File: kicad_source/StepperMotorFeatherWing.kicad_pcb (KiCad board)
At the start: 2 copper layers, 100 x 60 mm, 120 parts, among them CN1 ADAFRUIT_FEATHER, CN10 CONN_01X04, CN11 CONN_01X05, CN20 CONN_01X04, CN21 CONN_01X05, P1 WR-TBL_691322310002, P10 CONN_01X04, P2 WR-TBL_691313710002, P7 CONN_01X04, P8 CONN_01X04, P9 CONN_01X04, Q1 IPD90P03P4L- 04, U1 TMC5130A-TA, U2 TMC5130A-TA, U3 LT1085, U4 LM75, U9 IFX91041EJV, Y1 oscillator

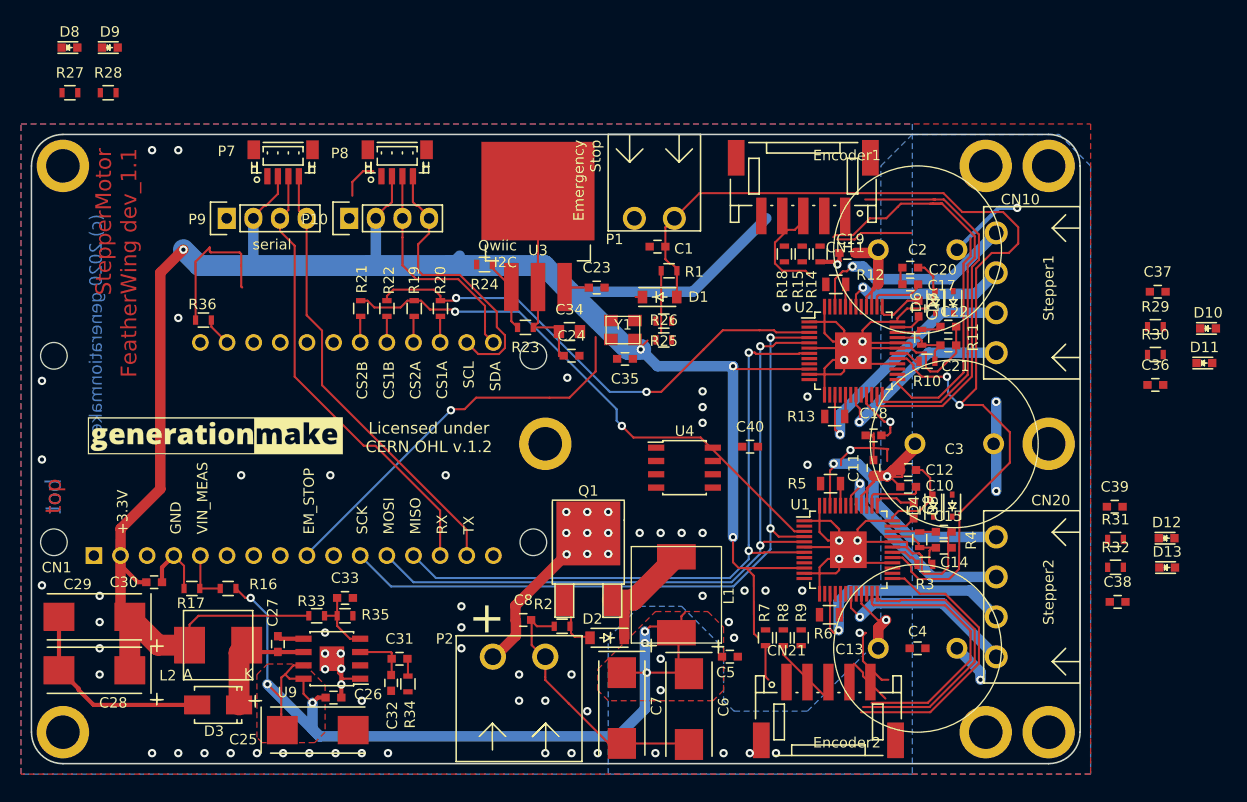
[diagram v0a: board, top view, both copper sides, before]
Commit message: updated layout
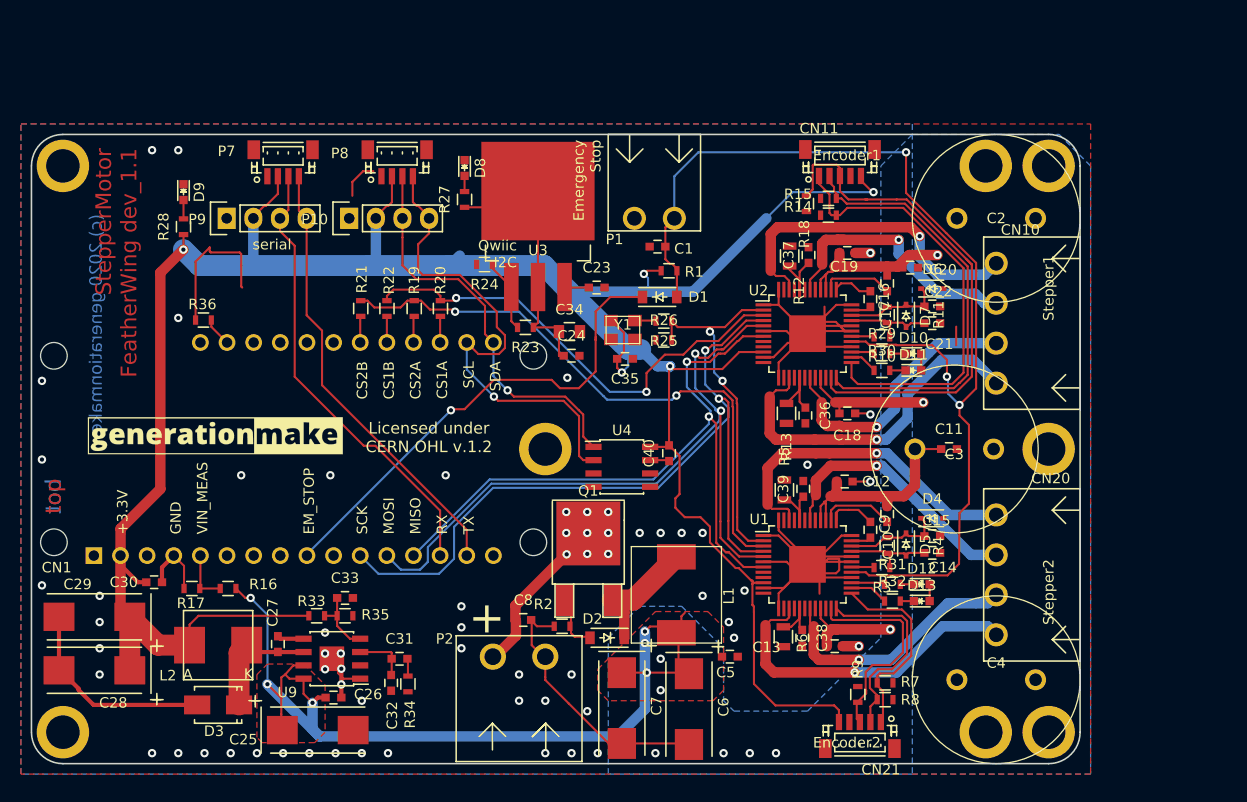
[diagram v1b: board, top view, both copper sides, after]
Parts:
- CN11, CN21: footprint connectors_JST_PH:Connectors_JST_S5B-PH-SM4-TB -> connectors_JST_SH:Connectors_JST_BM05B-SRSS-TB
- moved G*** 47.2 mm to (138.1, 62.4)
- moved D8 39.4 mm to (92.3, 69.2), turned to 270 degrees
- moved R27 39.0 mm to (92.3, 72.2), turned to 90 degrees
- moved C36 33.5 mm to (124.8, 92.8), turned to 270 degrees
- moved C37 33.5 mm to (125.1, 77.5), turned to 90 degrees
- moved C38 30.3 mm to (124.5, 114.0), turned to 270 degrees
- moved C39 29.7 mm to (124.6, 99.8), turned to 90 degrees
- moved D10 28.2 mm to (135.1, 86.9)
- moved D11 27.8 mm to (135.1, 88.5)
- moved R29 26.2 mm to (132.1, 86.9)
- moved R30 26.1 mm to (132.1, 88.5)
- moved D12 23.8 mm to (135.9, 108.9)
- moved D13 23.6 mm to (135.9, 110.5)
- moved R31 21.7 mm to (133.1, 108.9)
- moved R32 21.5 mm to (133.1, 110.5)
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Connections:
- CN10 pad 1: /MotorDriver1/OB2 -> /MotorDriver1/OB1
- CN10 pad 2: /MotorDriver1/OB1 -> /MotorDriver1/OB2
- CN20 pad 1: /MotorDriver2/OB2 -> /MotorDriver2/OB1
- CN20 pad 2: /MotorDriver2/OB1 -> /MotorDriver2/OB2
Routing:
- net GND: track 235.2 -> 167.7 mm, vias 77 -> 59
- net CLK_16M: track 0.00 -> 34.8 mm, vias 0 -> 2
- net +3V3: track 217.6 -> 247.9 mm, vias 4 -> 5
- net I2C_SCL: track 27.4 -> 47.8 mm, vias 0 -> 1
- net VIN: track 139.9 -> 158.8 mm
- net I2C_SDA: track 21.8 -> 38.6 mm, vias 0 -> 1
- net /MotorDriver2/ENCB: track 32.8 -> 19.7 mm
- net /MotorDriver1/ENCA: track 29.6 -> 42.3 mm
- net /MotorDriver2/ENCA: track 30.2 -> 19.0 mm
- net /MotorDriver1/OA1: track 20.8 -> 31.8 mm
- net /MotorDriver1/OA2: track 15.9 -> 25.8 mm
- net /MotorDriver1/OB1: track 24.8 -> 33.9 mm
- net /MotorDriver2/OA1: track 23.7 -> 31.5 mm
- net EM_STOP_D: track 38.8 -> 46.6 mm
- net +5V: track 18.6 -> 26.2 mm
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
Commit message: update layout
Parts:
- moved G*** 50.5 mm to (107.0, 102.2)
- moved R9 10.1 mm to (119.7, 120.0), turned to 180 degrees
- moved CN21 10.0 mm to (120.0, 123.3)
- moved R18 8.20 mm to (116.7, 72.4)
- moved CN11 8.10 mm to (120.0, 68.7)
- moved C40 7.98 mm to (119.6, 94.7)
- moved U4 7.89 mm to (115.0, 96.0)
- moved R8 7.39 mm to (125.6, 122.8), turned to 270 degrees
- moved R7 6.65 mm to (127.5, 122.8), turned to 270 degrees
- moved R14 5.22 mm to (128.5, 68.7), turned to 270 degrees
- moved R15 3.41 mm to (126.7, 68.7), turned to 270 degrees
- moved C2 2.24 mm to (145.0, 73.0)
- moved C36 2.11 mm to (124.6, 90.7)
- moved C4 2.00 mm to (145.0, 118.0)
- moved R13 1.71 mm to (122.8, 90.9)
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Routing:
- net +5V: track 26.2 -> 102.5 mm, vias 0 -> 2
- net +3V3: track 247.9 -> 306.7 mm, vias 5 -> 8
- net VIN: track 158.8 -> 209.9 mm, vias 11 -> 13
- net GND: track 167.7 -> 194.2 mm, vias 59 -> 98
- net /MotorDriver2/ENCN: track 20.4 -> 30.6 mm
- net /MotorDriver1/ENCB: track 41.6 -> 51.5 mm
- net /MotorDriver2/ENCB: track 19.7 -> 29.1 mm
- net /MotorDriver1/ENCN: track 50.9 -> 59.6 mm
- net /MotorDriver2/ENCA: track 19.0 -> 27.4 mm
- net /MotorDriver1/ENCA: track 42.3 -> 50.6 mm
- net I2C_SDA: track 38.6 -> 44.3 mm
- net I2C_SCL: track 47.8 -> 52.6 mm
- net CLK_16M: track 34.8 -> 37.6 mm
- net EM_STOP: track 105.1 -> 102.7 mm
- net /MotorDriver1/OA1: track 31.8 -> 29.7 mm
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
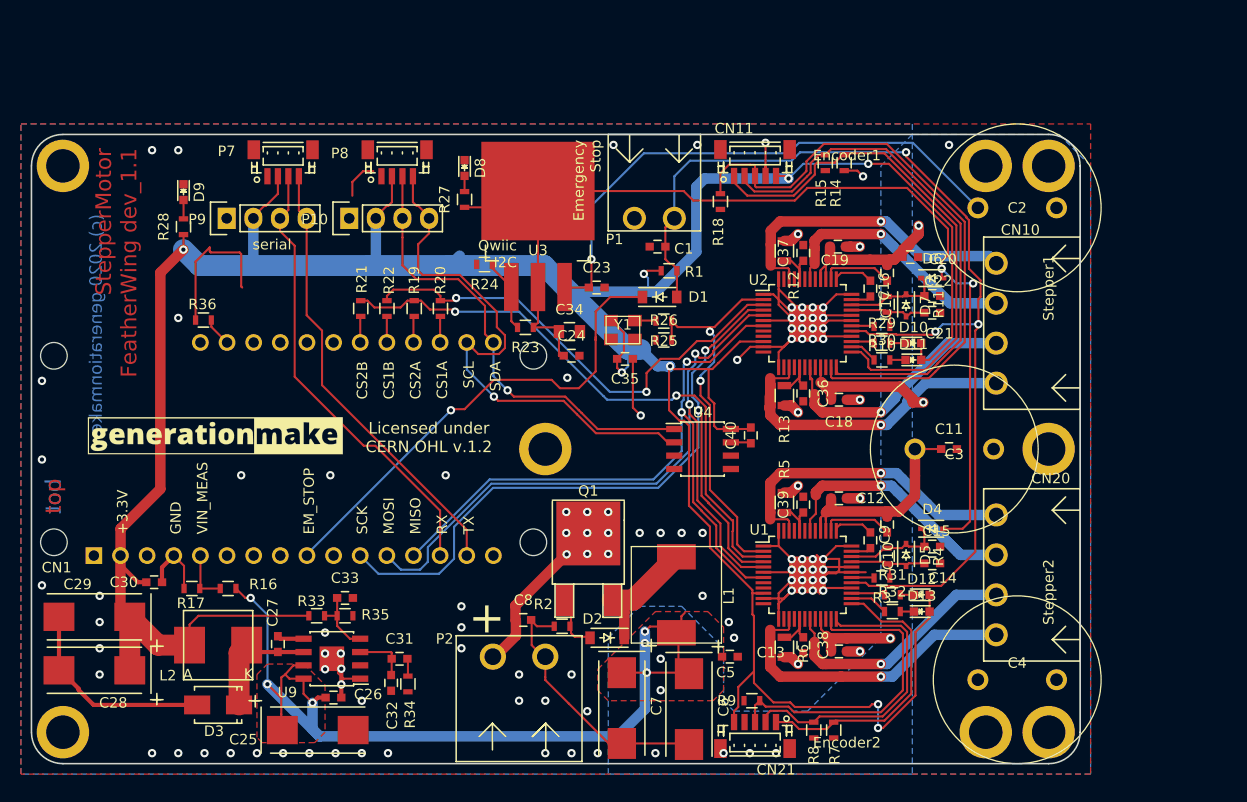
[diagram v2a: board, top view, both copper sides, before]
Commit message: updated layout
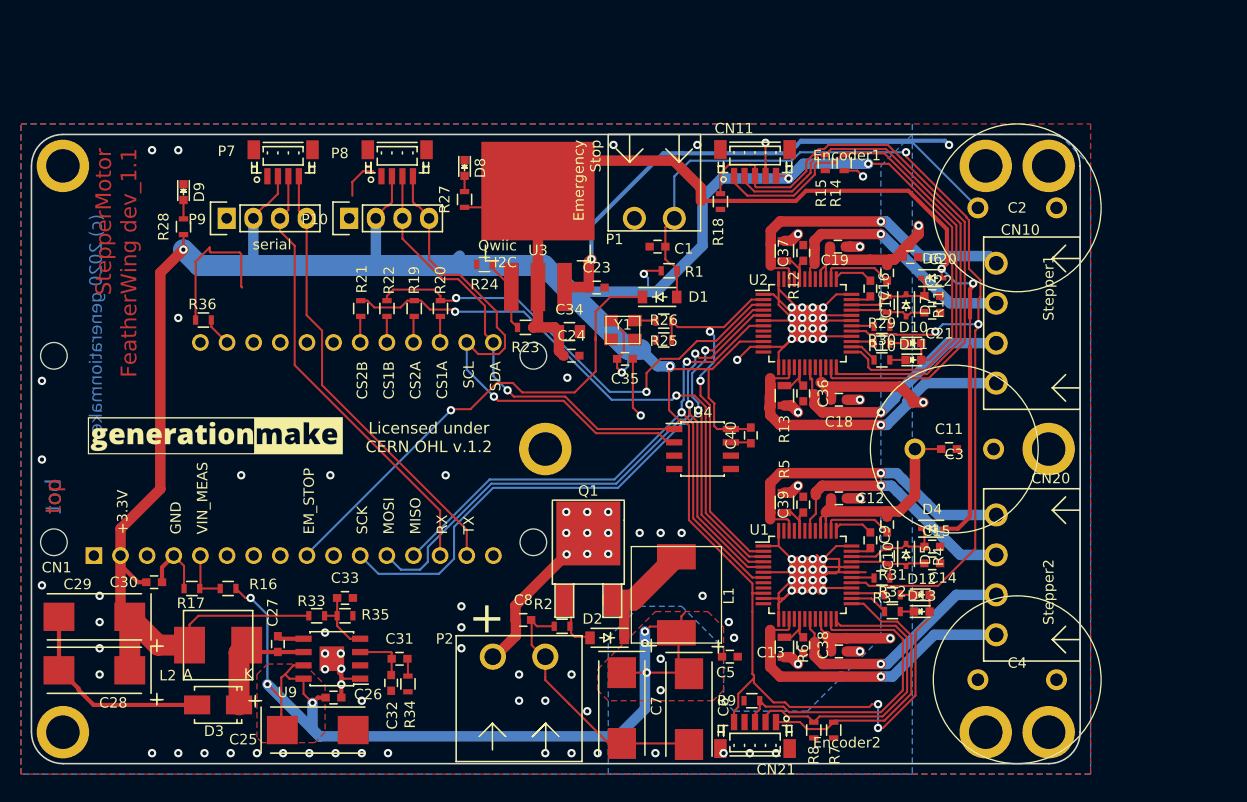
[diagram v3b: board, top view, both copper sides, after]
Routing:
- net VIN: track 209.9 -> 225.1 mm
- net +5V: track 102.5 -> 108.2 mm
- net MISO: track 67.1 -> 64.6 mm
- net MOSI: track 72.6 -> 70.2 mm
- net SCK: track 75.1 -> 72.8 mm
- net I2C_SCL: track 52.6 -> 50.5 mm
- net I2C_SDA: track 44.3 -> 42.8 mm
- net +3V3: track 306.7 -> 305.3 mm
- net /SER_RX: track 43.5 -> 42.8 mm
- net GND: vias 98 -> 97

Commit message: added expansion connector, updated layout
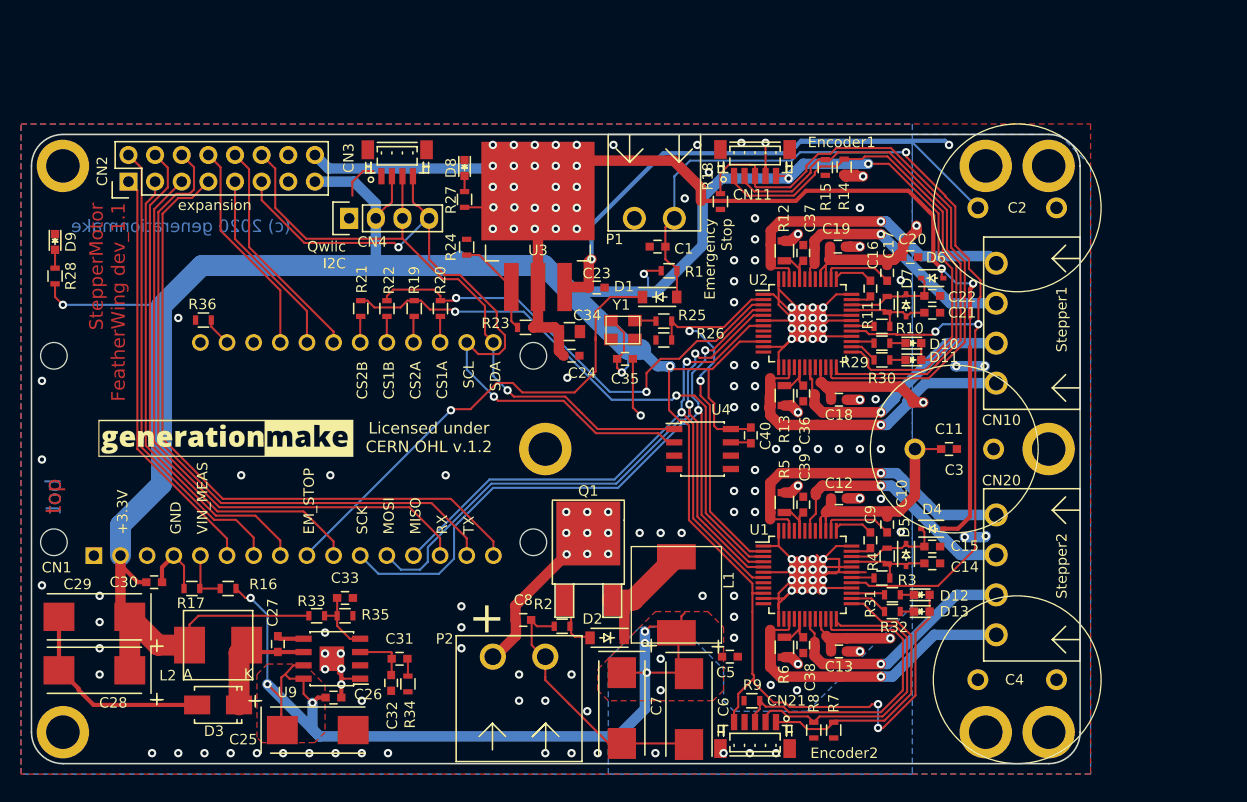
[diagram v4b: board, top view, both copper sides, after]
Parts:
- removed G***: generationmake_logo, labels:generationmake_logo
- removed G*** (x2): generationmake_small_solder, labels:generationmake_small_solder
- removed P7: CONN_01X04, connectors_JST_SH:Connectors_JST_BM04B-SRSS-TB
- removed P9: CONN_01X04, pin_headers:Pin_Header_Straight_1x04
- added CN2: CONN_02X08, pin_headers:Pin_Header_Straight_2x08, F.Cu at (60.2, 70.5)
- added L3: Label, labels:generationmake_logo, F.Cu at (69.5, 100.2)
- added L4: Label, labels:generationmake_small_solder, F.Cu at (90.0, 112.0)
- moved D9 13.1 mm to (53.2, 76.2)
- moved R28 13.1 mm to (53.2, 79.5)
- moved R24 2.37 mm to (92.5, 76.8), turned to 90 degrees
- moved R15 0.45 mm to (126.7, 69.2)
- moved R14 0.40 mm to (128.5, 69.1)
- renumbered P8 to CN3, P10 to CN4
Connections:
- CN1 pad 10: (no net) -> /A5
- CN1 pad 16: (no net) -> /P16
- CN1 pad 23: (no net) -> /P23
- CN1 pad 24: (no net) -> /P24
- CN1 pad 25: (no net) -> /P25
- CN1 pad 6: (no net) -> /A1
- CN1 pad 7: (no net) -> /A2
- CN1 pad 8: (no net) -> /A3
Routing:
- net /P16: track 0.00 -> 64.0 mm
- net /A5: track 0.00 -> 51.5 mm
- net /A2: track 0.00 -> 44.4 mm
- net /A3: track 0.00 -> 43.5 mm
- net /A1: track 0.00 -> 39.6 mm
- net /SER_TX: track 42.8 -> 64.8 mm
- net /P23: track 0.00 -> 21.8 mm
- net I2C_SCL: track 50.5 -> 71.3 mm, vias 1 -> 2
- net /P25: track 0.00 -> 20.7 mm
- net +5V: track 108.2 -> 127.7 mm, vias 2 -> 26
- net I2C_SDA: track 42.8 -> 61.8 mm
- net /P24: track 0.00 -> 18.2 mm
- net /SER_RX: track 42.8 -> 58.7 mm
- net GND: track 194.2 -> 183.7 mm, vias 97 -> 132
- net +3V3: track 305.3 -> 310.7 mm
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- added copper zone on B.Cu, net +5V
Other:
- board text added: "expansion"
- board text removed: "serial"

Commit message: updated part numbers
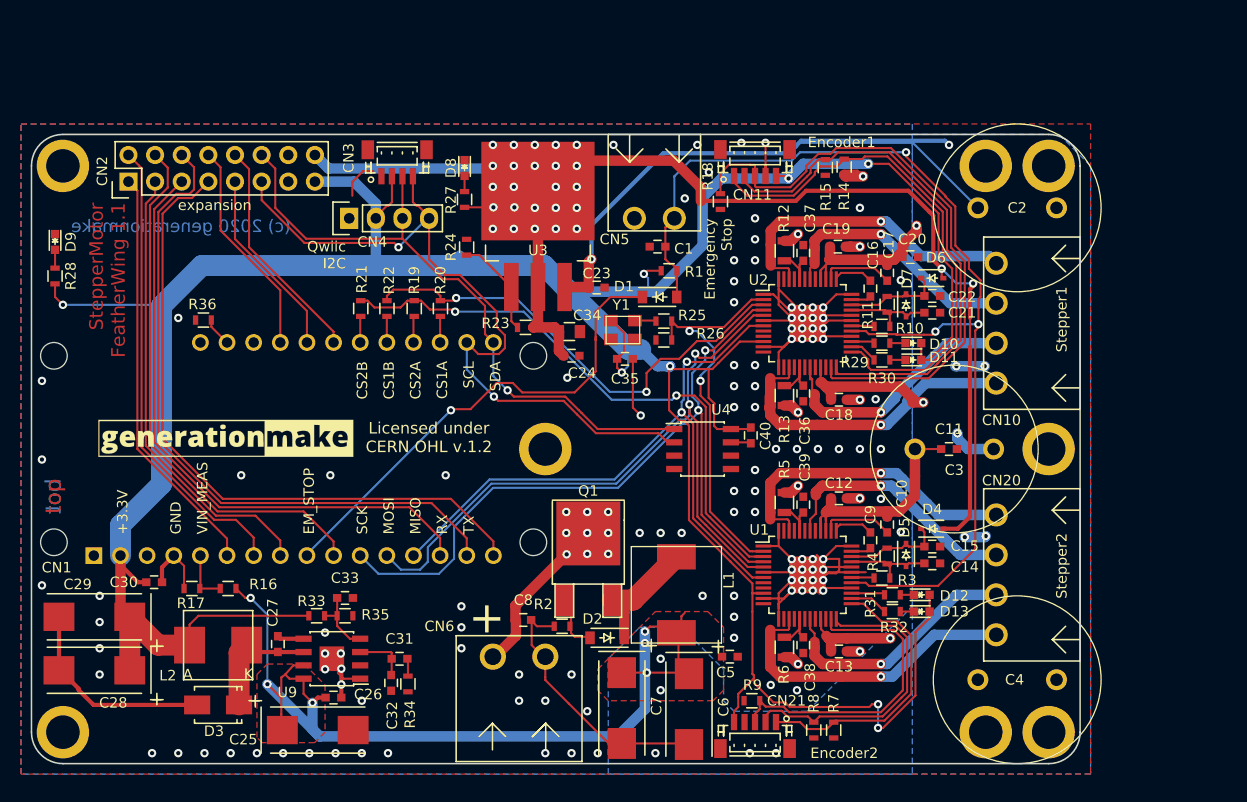
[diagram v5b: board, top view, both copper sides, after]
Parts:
- CN10, CN20: value CONN_01X04 -> 691322310004
- CN11, CN21: value CONN_01X05 -> BM05B-SRSS-TB
- CN2: value CONN_02X08 -> DNI
- CN3: value CONN_01X04 -> BM04B-SRSS-TB
- D10, D12: value Led_Small -> 150060GS75000
- D11, D13: value Led_Small -> 150060RS75000
- D8, D9: value Led_Small -> 150060BS75000
- U3: value LT1085 -> LT1085CM#PBF
- U4: value LM75 -> LM75BD
- Y1: value oscillator -> ECS-3225MV-160-BN-TR
- renumbered P1 to CN5, P2 to CN6
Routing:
- net GND: track 183.7 -> 188.0 mm, vias 132 -> 133
- net (no net): vias 1 -> 0
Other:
- board text added: "StepperMotor FeatherWing 1.1"
- board text removed: "StepperMotor FeatherWing dev_1.1"

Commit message: updated part numbers
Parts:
- C16, C9: value 22nF/63V -> 22nF 63V
- CN5: value WR-TBL_691322310002 -> 691322310002
- CN6: value WR-TBL_691313710002 -> 691313710002
- U3: value LT1085CM#PBF -> LM1085ISX-ADJ/NOPB
